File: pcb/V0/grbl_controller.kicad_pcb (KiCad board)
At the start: 2 copper layers, 54.6 x 80.6 mm, 44 parts, among them J1 DA15_Plug_MountingHoles, U1 firebeetle_esp32, U2 EL817, U3 EL817, U4 EL817, U5 EL817, U6 74LS07, U7 74LS07

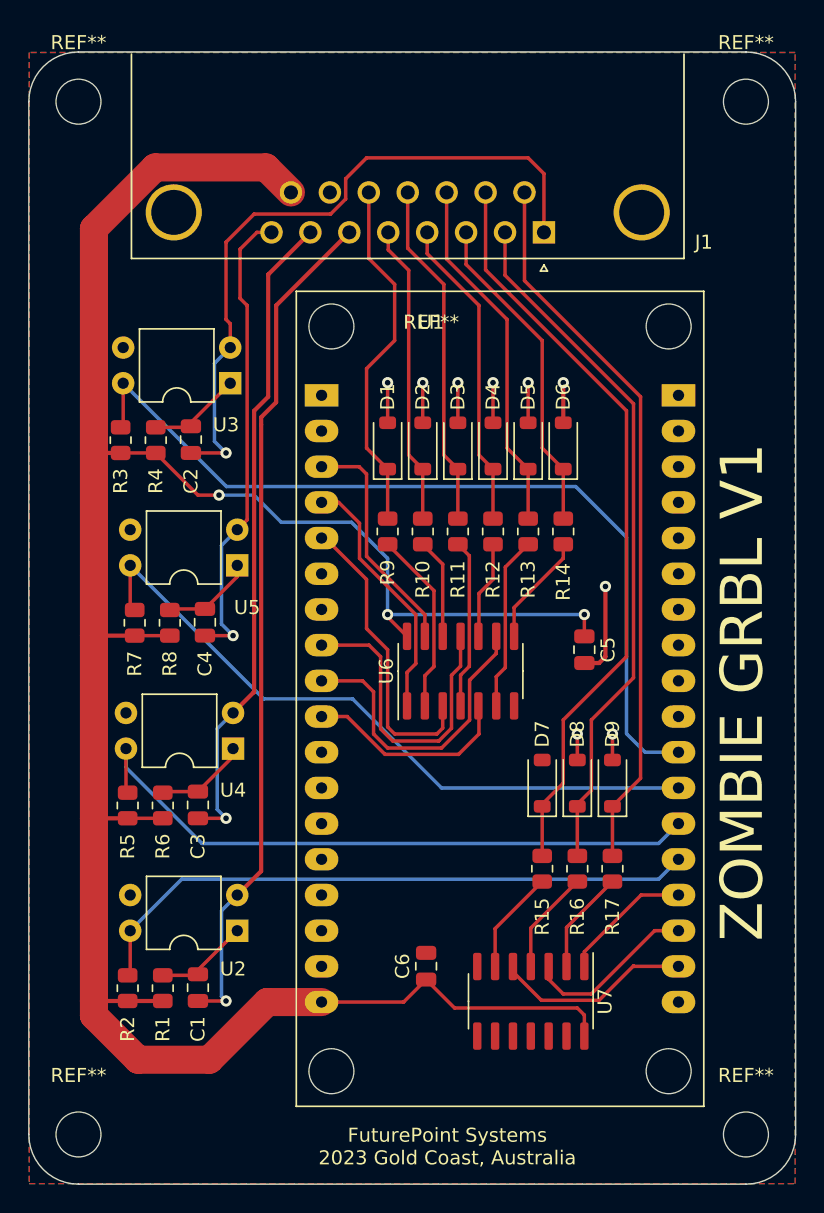
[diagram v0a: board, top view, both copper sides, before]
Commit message: Updated firebeetle mounting holes.
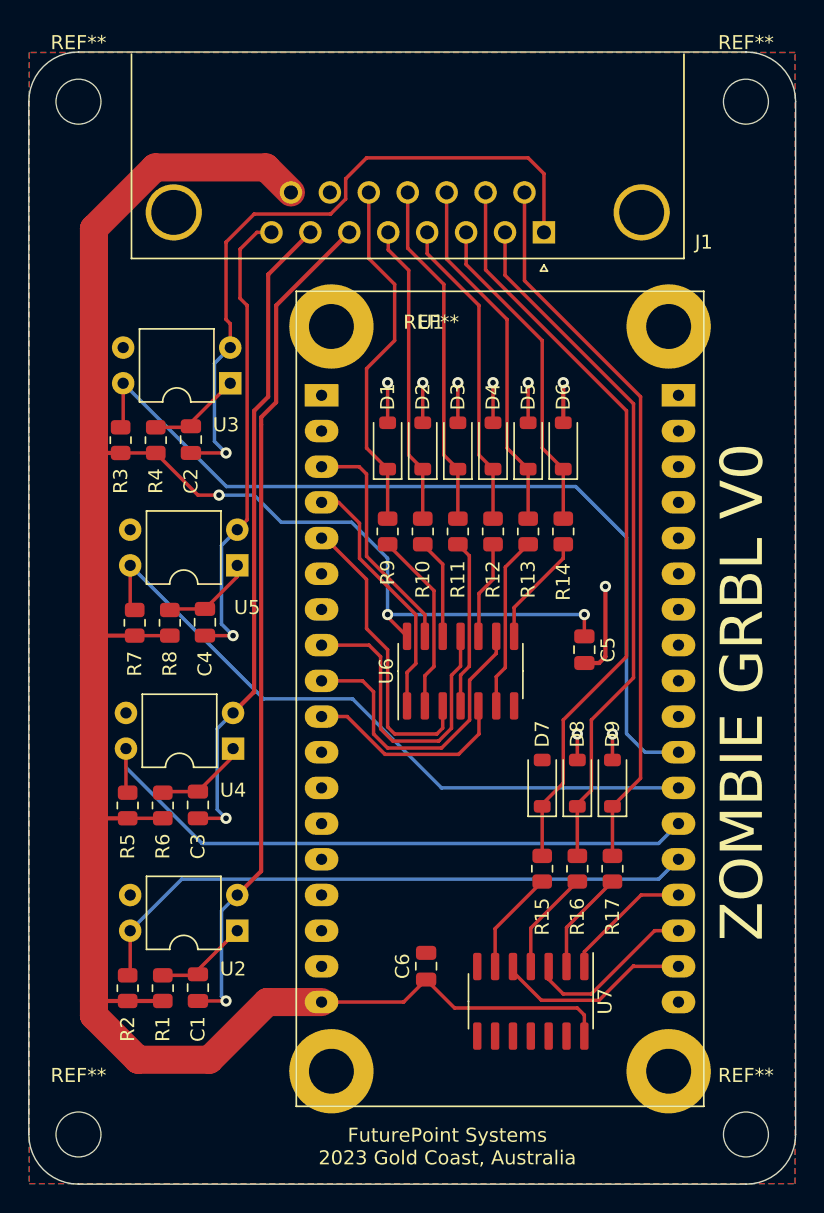
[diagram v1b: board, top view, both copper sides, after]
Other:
- board text added: "ZOMBIE GRBL V0"
- board text removed: "ZOMBIE GRBL V1"
